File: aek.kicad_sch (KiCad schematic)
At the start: 232 parts, among them J1 Conn_01x04_MountingPin, SW1 SW_Push, U1 ATmega32U4-AU, Y1 16MHz

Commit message: extension for buzzer from PF0
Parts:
- added BUZ1: Buzzer, Buzzer_Beeper:Buzzer_TDK_PS1240P02BT_D12.2mm_H6.5mm, symbol Device:R_Small
- C7: value 10F -> 10uF
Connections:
- net GND: now also BUZ1.2
- net BUZIN: now reaches U1.41 (PF0)
- net BUZIN: now also BUZ1.1
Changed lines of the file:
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@@
     (stroke (width 0) (type solid) (color 0 0 0 0))
   )
+  (wire (pts (xy 91.44 196.85) (xy 91.44 200.66))
+    (stroke (width 0) (type solid) (color 0 0 0 0))
+  )
+  (wire (pts (xy 91.44 196.85) (xy 95.25 196.85))
+    (stroke (width 0) (type solid) (color 0 0 0 0))
+  )
+  (wire (pts (xy 100.33 196.85) (xy 105.41 196.85))
+    (stroke (width 0) (type solid) (color 0 0 0 0))
+  )
   (wire (pts (xy 100.33 233.68) (xy 100.33 241.3))
     (stroke (width 0) (type solid) (color 0 0 0 0))
@@
     )
   )
+  (global_label "BUZIN" (shape input) (at 87.63 120.65 0) (fields_autoplaced)
+    (effects (font (size 1.27 1.27)) (justify left))
+    (property "Intersheet References" "${INTERSHEET_REFS}" (id 0) (at 95.6486 120.5706 0)
+      (effects (font (size 1.27 1.27)) (justify left) hide)
+    )
+  )
   (global_label "COL0" (shape input) (at 87.63 128.27 0) (fields_autoplaced)
     (effects (font (size 1.27 1.27)) (justify left))
@@
     )
   )
+  (global_label "BUZIN" (shape input) (at 105.41 196.85 0) (fields_autoplaced)
+    (effects (font (size 1.27 1.27)) (justify left))
+    (property "Intersheet References" "${INTERSHEET_REFS}" (id 0) (at 113.4286 196.7706 0)
+      (effects (font (size 1.27 1.27)) (justify left) hide)
+    )
+  )
   (global_label "LEDDIN" (shape input) (at 107.95 129.54 0) (fields_autoplaced)
     (effects (font (size 1.27 1.27)) (justify left))
@@
     (pin "1")
   )
+  (symbol (lib_id "power:GND") (at 91.44 200.66 0) (unit 1)
+    (in_bom yes) (on_board yes)
+    (property "Reference" "#PWR0115" (id 0) (at 91.44 207.01 0)
+      (effects (font (size 1.27 1.27)) hide)
+    )
+    (property "Value" "GND" (id 1) (at 91.567 205.0542 0))
+    (property "Footprint" "" (id 2) (at 91.44 200.66 0)
+      (effects (font (size 1.27 1.27)) hide)
+    )
+    (property "Datasheet" "" (id 3) (at 91.44 200.66 0)
+      (effects (font (size 1.27 1.27)) hide)
+    )
+    (pin "1")
+  )
   (symbol (lib_id "power:GND") (at 110.49 241.3 90) (unit 1)
     (in_bom yes) (on_board yes)
@@
     (pin "2")
   )
+  (symbol (lib_id "Device:R_Small") (at 97.79 196.85 270) (unit 1)
+    (in_bom yes) (on_board yes)
+    (property "Reference" "BUZ1" (id 0) (at 97.79 191.8716 90))
+    (property "Value" "Buzzer" (id 1) (at 97.79 194.183 90))
+    (property "Footprint" "Buzzer_Beeper:Buzzer_TDK_PS1240P02BT_D12.2mm_H6.5mm" (id 2) (at 97.79 196.85 0)
+      (effects (font (size 1.27 1.27)) hide)
+    )
+    (property "Datasheet" "~" (id 3) (at 97.79 196.85 0)
+      (effects (font (size 1.27 1.27)) hide)
+    )
+    (pin "1")
+    (pin "2")
+  )
   (symbol (lib_id "Device:R_Small") (at 100.33 125.73 270) (unit 1)
     (in_bom yes) (on_board yes)
@@
       (effects (font (size 1.27 1.27)) (justify left))
     )
-    (property "Value" "10F" (id 1) (at 53.1368 116.713 0)
+    (property "Value" "10uF" (id 1) (at 53.1368 116.713 0)
       (effects (font (size 1.27 1.27)) (justify left))
     )
@@
       (reference "#PWR0114") (unit 1) (value "GND") (footprint "")
     )
+    (path "/3e62c537-1a1c-4663-a609-5d9c22d04c8d"
+      (reference "#PWR0115") (unit 1) (value "GND") (footprint "")
+    )
     (path "/00000000-0000-0000-0000-000062f02ba2"
       (reference "#PWR0116") (unit 1) (value "+5V") (footprint "")
@@
       (reference "#PWR0122") (unit 1) (value "GND") (footprint "")
     )
+    (path "/5e7696e2-7dd3-4741-abb9-0ce915833473"
+      (reference "BUZ1") (unit 1) (value "Buzzer") (footprint "Buzzer_Beeper:Buzzer_TDK_PS1240P02BT_D12.2mm_H6.5mm")
+    )
     (path "/00000000-0000-0000-0000-00006120a5a3"
       (reference "C1") (unit 1) (value "0.1uF") (footprint "Capacitor_SMD:C_0805_2012Metric")
@@
     )
     (path "/00000000-0000-0000-0000-00006121f298"
-      (reference "C7") (unit 1) (value "10F") (footprint "Capacitor_SMD:C_0805_2012Metric")
+      (reference "C7") (unit 1) (value "10uF") (footprint "Capacitor_SMD:C_0805_2012Metric")
     )
     (path "/00000000-0000-0000-0000-00006137af7c"

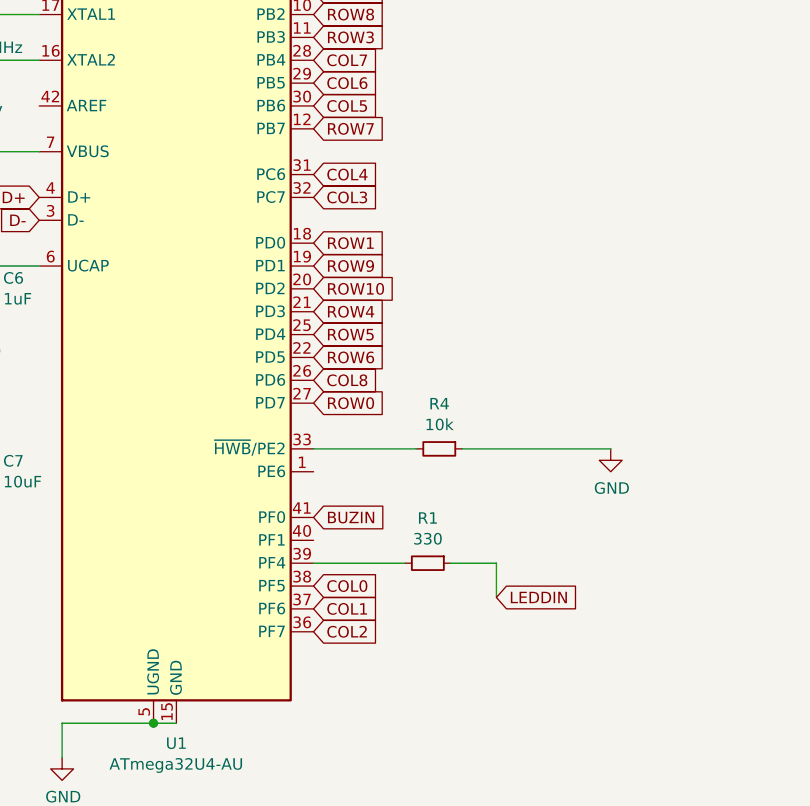
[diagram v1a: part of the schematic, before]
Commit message: cleanup and gitignore aek-backups
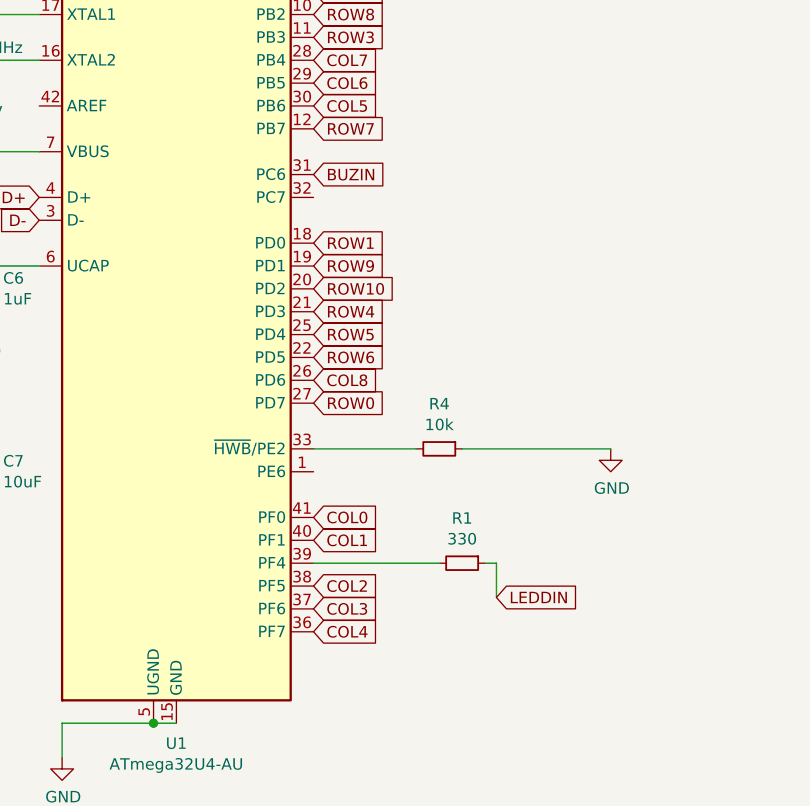
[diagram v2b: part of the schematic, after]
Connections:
- net BUZIN: now also U1.31 (PC6); no longer U1.41 (PF0)
- net COL0: now also U1.41 (PF0); no longer U1.38 (PF5)
- net COL1: now also U1.40 (PF1); no longer U1.37 (PF6)
- net COL2: now also U1.38 (PF5); no longer U1.36 (PF7)
- net COL3: now also U1.37 (PF6); no longer U1.32 (PC7)
- net COL4: now also U1.36 (PF7); no longer U1.31 (PC6)
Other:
- moved on the sheet: R1
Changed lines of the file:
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@@
     (stroke (width 0) (type solid) (color 0 0 0 0))
   )
-  (wire (pts (xy 87.63 125.73) (xy 97.79 125.73))
+  (wire (pts (xy 87.63 125.73) (xy 101.6 125.73))
     (stroke (width 0) (type solid) (color 0 0 0 0))
   )
@@
     (stroke (width 0) (type solid) (color 0 0 0 0))
   )
-  (wire (pts (xy 102.87 125.73) (xy 107.95 125.73))
-    (stroke (width 0) (type solid) (color 0 0 0 0))
-  )
   (wire (pts (xy 104.14 113.03) (xy 120.65 113.03))
     (stroke (width 0) (type solid) (color 0 0 0 0))
   )
   (wire (pts (xy 105.41 241.3) (xy 110.49 241.3))
+    (stroke (width 0) (type solid) (color 0 0 0 0))
+  )
+  (wire (pts (xy 106.68 125.73) (xy 107.95 125.73))
     (stroke (width 0) (type solid) (color 0 0 0 0))
   )
@@
     )
   )
-  (global_label "COL4" (shape input) (at 87.63 82.55 0) (fields_autoplaced)
-    (effects (font (size 1.27 1.27)) (justify left))
-    (property "Intersheet References" "${INTERSHEET_REFS}" (id 0) (at 7.62 -41.91 0)
-      (effects (font (size 1.27 1.27)) hide)
-    )
-  )
-  (global_label "COL3" (shape input) (at 87.63 85.09 0) (fields_autoplaced)
-    (effects (font (size 1.27 1.27)) (justify left))
-    (property "Intersheet References" "${INTERSHEET_REFS}" (id 0) (at 7.62 -41.91 0)
-      (effects (font (size 1.27 1.27)) hide)
+  (global_label "BUZIN" (shape input) (at 87.63 82.55 0) (fields_autoplaced)
+    (effects (font (size 1.27 1.27)) (justify left))
+    (property "Intersheet References" "${INTERSHEET_REFS}" (id 0) (at 95.6486 82.4706 0)
+      (effects (font (size 1.27 1.27)) (justify left) hide)
     )
   )
@@
     )
   )
-  (global_label "BUZIN" (shape input) (at 87.63 120.65 0) (fields_autoplaced)
-    (effects (font (size 1.27 1.27)) (justify left))
-    (property "Intersheet References" "${INTERSHEET_REFS}" (id 0) (at 95.6486 120.5706 0)
-      (effects (font (size 1.27 1.27)) (justify left) hide)
-    )
-  )
-  (global_label "COL0" (shape input) (at 87.63 128.27 0) (fields_autoplaced)
-    (effects (font (size 1.27 1.27)) (justify left))
-    (property "Intersheet References" "${INTERSHEET_REFS}" (id 0) (at 7.62 -41.91 0)
-      (effects (font (size 1.27 1.27)) hide)
-    )
-  )
-  (global_label "COL1" (shape input) (at 87.63 130.81 0) (fields_autoplaced)
-    (effects (font (size 1.27 1.27)) (justify left))
-    (property "Intersheet References" "${INTERSHEET_REFS}" (id 0) (at 7.62 -41.91 0)
-      (effects (font (size 1.27 1.27)) hide)
-    )
-  )
-  (global_label "COL2" (shape input) (at 87.63 133.35 0) (fields_autoplaced)
-    (effects (font (size 1.27 1.27)) (justify left))
-    (property "Intersheet References" "${INTERSHEET_REFS}" (id 0) (at 7.62 -41.91 0)
+  (global_label "COL0" (shape input) (at 87.63 120.65 0) (fields_autoplaced)
+    (effects (font (size 1.27 1.27)) (justify left))
+    (property "Intersheet References" "${INTERSHEET_REFS}" (id 0) (at 7.62 -49.53 0)
+      (effects (font (size 1.27 1.27)) hide)
+    )
+  )
+  (global_label "COL1" (shape input) (at 87.63 123.19 0) (fields_autoplaced)
+    (effects (font (size 1.27 1.27)) (justify left))
+    (property "Intersheet References" "${INTERSHEET_REFS}" (id 0) (at 7.62 -49.53 0)
+      (effects (font (size 1.27 1.27)) hide)
+    )
+  )
+  (global_label "COL2" (shape input) (at 87.63 128.27 0) (fields_autoplaced)
+    (effects (font (size 1.27 1.27)) (justify left))
+    (property "Intersheet References" "${INTERSHEET_REFS}" (id 0) (at 7.62 -46.99 0)
+      (effects (font (size 1.27 1.27)) hide)
+    )
+  )
+  (global_label "COL3" (shape input) (at 87.63 130.81 0) (fields_autoplaced)
+    (effects (font (size 1.27 1.27)) (justify left))
+    (property "Intersheet References" "${INTERSHEET_REFS}" (id 0) (at 7.62 3.81 0)
+      (effects (font (size 1.27 1.27)) hide)
+    )
+  )
+  (global_label "COL4" (shape input) (at 87.63 133.35 0) (fields_autoplaced)
+    (effects (font (size 1.27 1.27)) (justify left))
+    (property "Intersheet References" "${INTERSHEET_REFS}" (id 0) (at 7.62 8.89 0)
       (effects (font (size 1.27 1.27)) hide)
     )
@@
     (pin "2")
   )
-  (symbol (lib_id "Device:R_Small") (at 100.33 125.73 270) (unit 1)
-    (in_bom yes) (on_board yes)
-    (property "Reference" "R1" (id 0) (at 100.33 120.7516 90))
-    (property "Value" "330" (id 1) (at 100.33 123.063 90))
-    (property "Footprint" "Resistor_SMD:R_0805_2012Metric" (id 2) (at 100.33 125.73 0)
-      (effects (font (size 1.27 1.27)) hide)
-    )
-    (property "Datasheet" "~" (id 3) (at 100.33 125.73 0)
-      (effects (font (size 1.27 1.27)) hide)
-    )
-    (pin "1")
-    (pin "2")
-  )
   (symbol (lib_id "Device:R_Small") (at 101.6 113.03 270) (unit 1)
     (in_bom yes) (on_board yes)
@@
       (effects (font (size 1.27 1.27)) hide)
     )
+    (pin "1")
+    (pin "2")
+  )
+  (symbol (lib_id "Device:R_Small") (at 104.14 125.73 270) (unit 1)
+    (in_bom yes) (on_board yes)
+    (property "Reference" "R1" (id 0) (at 104.14 120.7516 90))
+    (property "Value" "330" (id 1) (at 104.14 123.063 90))
+    (property "Footprint" "Resistor_SMD:R_0805_2012Metric" (id 2) (at 104.14 125.73 0)
+      (effects (font (size 1.27 1.27)) hide)
+    )
+    (property "Datasheet" "~" (id 3) (at 104.14 125.73 0)
+      (effects (font (size 1.27 1.27)) hide)
+    )
